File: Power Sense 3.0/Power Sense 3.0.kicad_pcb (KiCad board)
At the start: 2 copper layers, 85.3 x 47.5 mm, 45 parts, among them IC1 MCP3909, J1 Power, J2 ProgHead, J3 SPI, T1 AC1030, T2 Murata_782485_55C, U1 PIC18F25K20_I/SS, Y1 3.579545MHz Crystal

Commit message: Updated files with new files
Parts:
- moved C7 33.6 mm to (108.6, 72.8)
- moved R18 25.9 mm to (117.3, 42.2), turned to 90 degrees
- moved C10 25.1 mm to (131.5, 50.1)
- moved R17 10.9 mm to (114.3, 40.4), turned to 90 degrees
- moved R15 9.01 mm to (131.3, 67.1), turned to 180 degrees
- moved C8 6.48 mm to (113.4, 59.1)
- moved R16 6.35 mm to (115.1, 67.7)
- moved C5 5.76 mm to (102.1, 61.8), turned to 270 degrees
- moved C6 3.54 mm to (101.7, 58.9), turned to 180 degrees
- moved T2 2.79 mm to (73.9, 49.3), turned to 90 degrees
- moved R11 1.59 mm to (102.0, 67.7)
- moved R21 1.28 mm to (122.4, 41.7)
- moved R20 1.21 mm to (122.4, 39.1)
- moved R19 1.15 mm to (122.4, 36.6)
- moved R14 0.83 mm to (105.3, 67.7)
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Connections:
- U1 pad 15: Net-(U1-Pad15) -> Net-(R18-Pad2)
- U1 pad 26: Net-(R18-Pad2) -> Net-(U1-Pad26)
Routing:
- net /+5V: track 0.00 -> 75.5 mm, vias 0 -> 2
- net /Fo0toPIC: track 0.00 -> 68.5 mm, vias 0 -> 2
- net /HFtoPIC: track 0.00 -> 61.1 mm, vias 0 -> 2
- net /LED_TO_11: track 0.00 -> 57.6 mm, vias 0 -> 2
- net /Fo1toPIC: track 0.00 -> 57.3 mm, vias 0 -> 2
- net /LED_TO_12: track 0.00 -> 51.7 mm, vias 0 -> 2
- net Net-(R2-Pad1): track 0.00 -> 49.8 mm
- net Net-(C10-Pad1): track 0.00 -> 49.0 mm, vias 0 -> 2
- net /LED_TO_25: track 0.00 -> 48.4 mm, vias 0 -> 2
- net Net-(R17-Pad2): track 0.00 -> 33.2 mm
- net /SDO: track 0.00 -> 30.3 mm, vias 0 -> 2
- net /SPI_CLK: track 0.00 -> 29.5 mm, vias 0 -> 2
- net /MCLR: track 0.00 -> 29.1 mm, vias 0 -> 2
- net Net-(R3-Pad2): track 0.00 -> 27.9 mm
- net /N: track 0.00 -> 24.2 mm
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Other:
- net class Default: clearance 0.508 -> 0.2032
- net class MCP added: clearance 0.2032, trace_width 0.4064, via_dia 1.6764, via_drill 0.7
- rule trace_clearance: 0.508 -> 0.2032

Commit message: Load Cap Change
Change load capacitors from 30 pF to 27 pF
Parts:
- C8, C9: value 30pF -> 27pF
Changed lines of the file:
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@@
       (effects (font (size 1 1) (thickness 0.15)))
     )
-    (fp_text value 30pF (at 1.25 2.11 270) (layer F.Fab)
+    (fp_text value 27pF (at 1.25 2.11 270) (layer F.Fab)
       (effects (font (size 1 1) (thickness 0.15)))
     )
@@
       (effects (font (size 1 1) (thickness 0.15)))
     )
-    (fp_text value 30pF (at 1.25 2.11 90) (layer F.Fab)
+    (fp_text value 27pF (at 1.25 2.11 90) (layer F.Fab)
       (effects (font (size 1 1) (thickness 0.15)))
     )

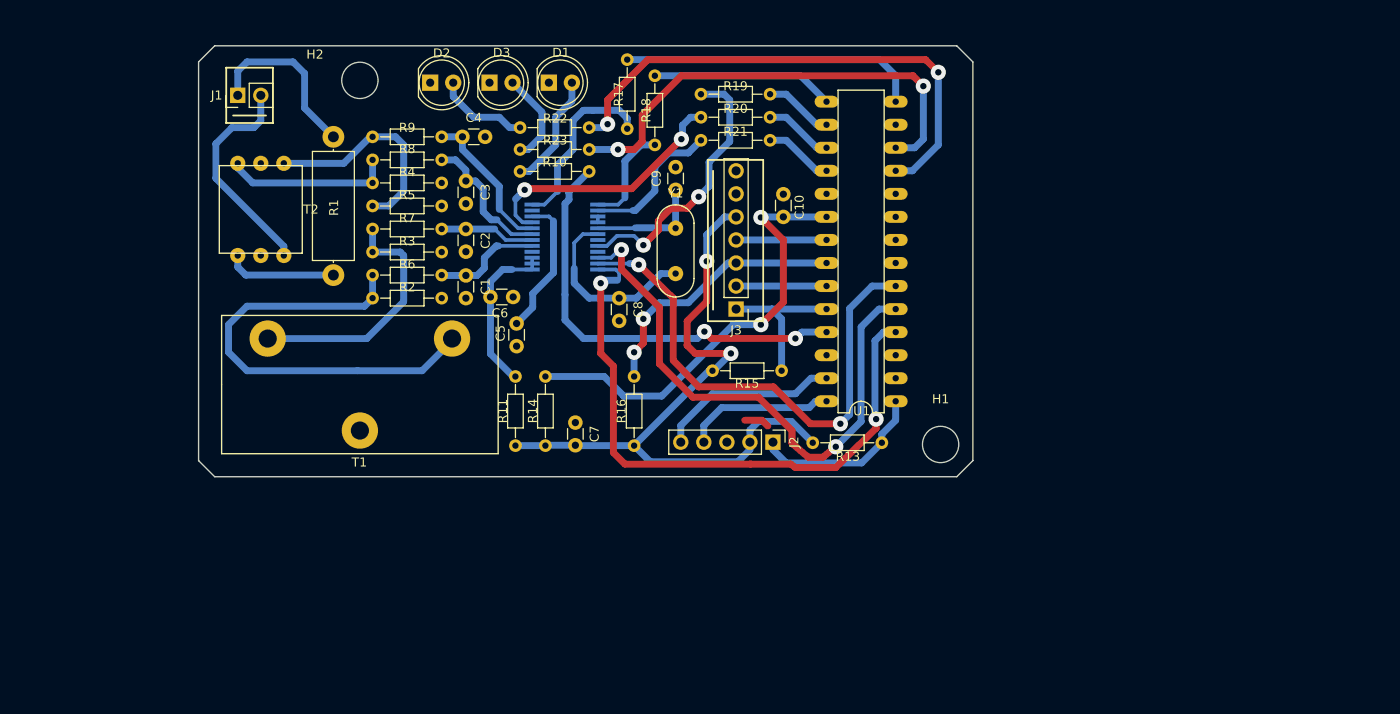
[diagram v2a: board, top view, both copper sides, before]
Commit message: PCB Layout Changes
Increased the width and height of the board slightly. Components were moved, and traces were redone.
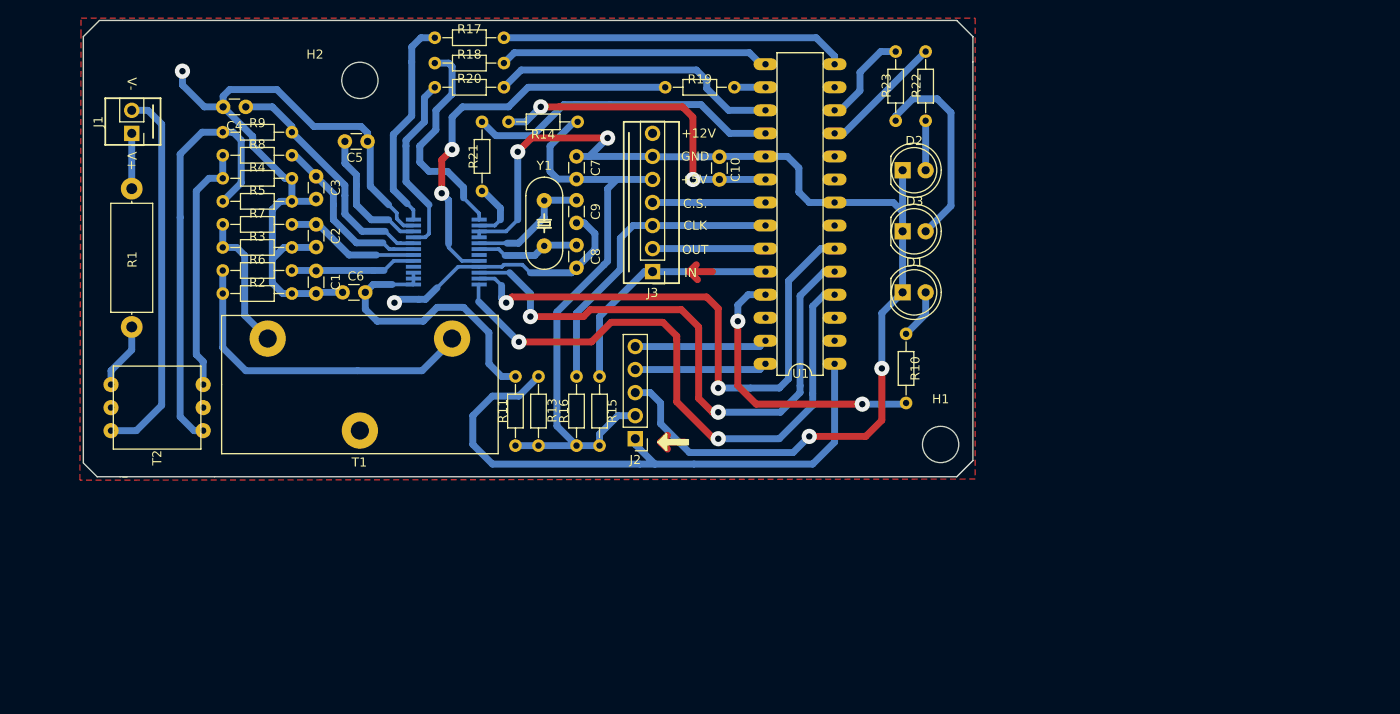
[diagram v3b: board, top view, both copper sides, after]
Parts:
- C8, C9: value 27pF -> 30pF
- moved D2 53.0 mm to (144.7, 45.0)
- moved D3 48.4 mm to (144.7, 51.7)
- moved R10 46.2 mm to (145.0, 63.0), turned to 270 degrees
- moved D1 45.3 mm to (144.7, 58.4)
- moved R22 44.7 mm to (147.2, 39.5), turned to 90 degrees
- moved R23 41.5 mm to (143.9, 39.5), turned to 90 degrees
- moved R13 30.2 mm to (104.5, 75.3), turned to 90 degrees
- moved R20 29.5 mm to (93.1, 35.8)
- moved C7 29.3 mm to (108.7, 43.4)
- moved R14 28.4 mm to (101.2, 39.6), turned to 0 degrees
- moved C5 27.6 mm to (83.2, 41.8), turned to 0 degrees
- moved R18 25.9 mm to (93.1, 33.1), turned to 0 degrees
- moved R21 24.8 mm to (98.3, 47.2), turned to 90 degrees
- moved T2 24.7 mm to (62.5, 71.1), turned to 0 degrees
- moved C4 24.1 mm to (72.3, 38.0), turned to 180 degrees
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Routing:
- net GND: track 0.65 -> 237.6 mm, vias 0 -> 6
- net /5V_PULL_UP: track 19.6 -> 66.3 mm
- net /LED_TO_11: track 57.6 -> 13.8 mm, vias 2 -> 0
- net /LED_TO_12: track 51.7 -> 10.6 mm, vias 2 -> 0
- net Net-(R21-Pad2): track 7.62 -> 34.6 mm
- net Net-(R5-Pad2): track 24.0 -> 47.8 mm
- net Net-(R20-Pad2): track 8.19 -> 32.0 mm
- net /N: track 24.2 -> 41.7 mm
- net /LED_TO_25: track 48.4 -> 31.8 mm
- net Net-(C6-Pad2): track 18.2 -> 32.0 mm
- net /SDO: track 30.3 -> 44.0 mm
- net Net-(R2-Pad1): track 49.8 -> 36.4 mm
- net /H: track 19.3 -> 6.10 mm
- net /SDI: track 11.4 -> 24.3 mm
- net Net-(C10-Pad1): track 49.0 -> 36.3 mm
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- added copper zone on F.Cu, net GND
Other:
- board size 85.3 x 47.5 mm -> 98 x 50.3 mm
- board text added: "+12V"
- board text added: "+5V"
- board text added: "C.S."
- board text added: "CLK"
- board text added: "GND"
- board text added: "IN"
- board text added: "OUT"
- board text added: "V+"
- board text added: "V-"

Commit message: Updated schematic for Power Sense
Updated schematic for Power Sense to include new transformer and resistor divider components.

**Incomplete PCB Layout**
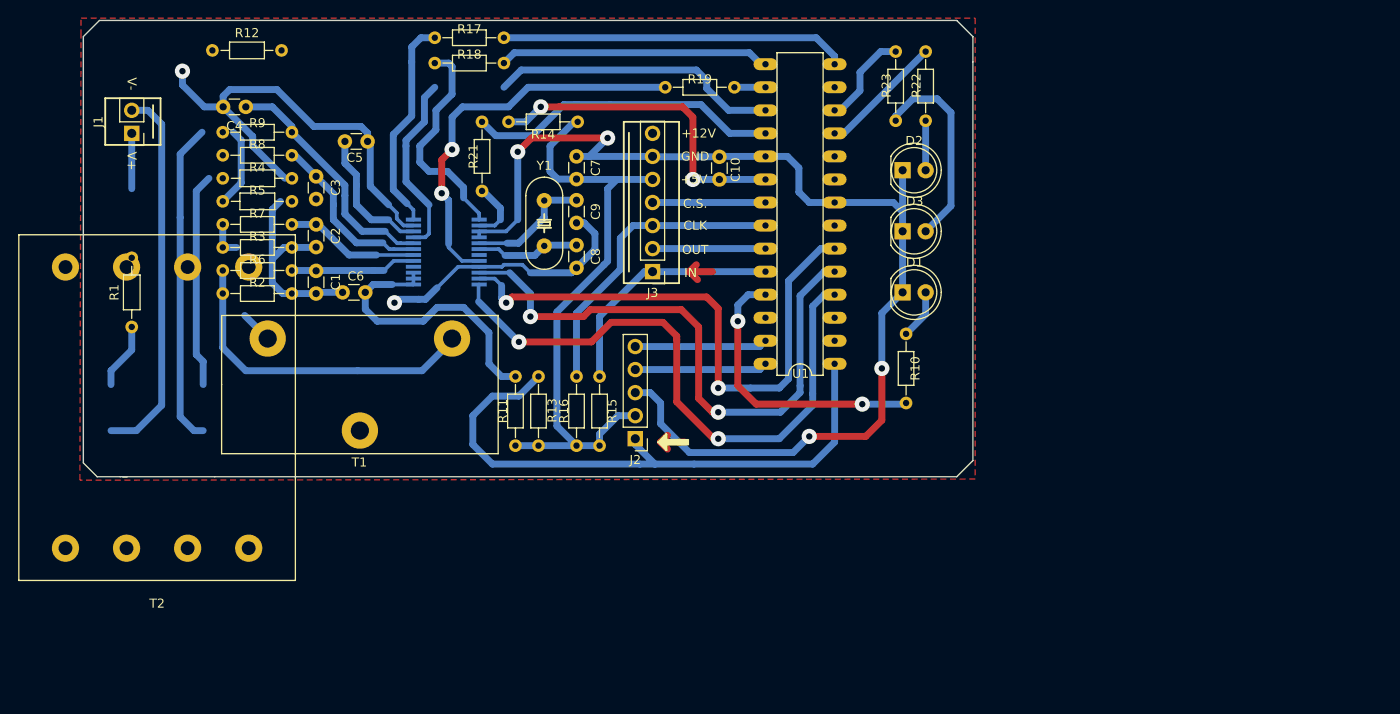
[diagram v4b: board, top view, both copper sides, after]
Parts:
- removed H1, H2: MountingHole_4mm, Mounting_Holes:MountingHole_4mm
- removed R20: 1k, Resistors_THT:R_Axial_DIN0204_L3.6mm_D1.6mm_P7.62mm_Horizontal
- added R12: 1k, Resistor_THT:R_Axial_DIN0204_L3.6mm_D1.6mm_P7.62mm_Horizontal, F.Cu at (68.6, 31.8)
- C8, C9: value 30pF -> 27pF
- R1: value 150k 1W -> 536k; footprint Resistors_THT:R_Axial_DIN0414_L11.9mm_D4.5mm_P15.24mm_Horizontal -> Resistor_THT:R_Axial_DIN0204_L3.6mm_D1.6mm_P7.62mm_Horizontal
- R4: value 200 1% -> 1k; footprint Resistors_THT:R_Axial_DIN0204_L3.6mm_D1.6mm_P7.62mm_Horizontal -> Resistor_THT:R_Axial_DIN0204_L3.6mm_D1.6mm_P7.62mm_Horizontal
- R5: value 200 1% -> 10k 1%; footprint Resistors_THT:R_Axial_DIN0204_L3.6mm_D1.6mm_P7.62mm_Horizontal -> Resistor_THT:R_Axial_DIN0204_L3.6mm_D1.6mm_P7.62mm_Horizontal
- T2: value Murata_782485_55C -> Transformer_1P_1S; footprint EMMS_FP:Murata_782485_Series -> EMMS_FP:Transformer FS12-090-C2
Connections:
- C4 pad 1: Net-(C4-Pad1) -> Net-(C3-Pad2)
- IC1 pad 8: Net-(C4-Pad1) -> Net-(C3-Pad2)
- J1 pad 2: /N -> GND
- R4 pad 1: Net-(R4-Pad1) -> GND
- R4 pad 2: GND -> Net-(R1-Pad1)
- R5 pad 1: GND -> Net-(R1-Pad1)
- R8 pad 1: Net-(R4-Pad1) -> Net-(R1-Pad1)
- R9 pad 1: Net-(R5-Pad2) -> GND
- R9 pad 2: Net-(C4-Pad1) -> Net-(C3-Pad2)
- T2 pad 1: Net-(R1-Pad1) -> /H
- T2 pad 2: Net-(T2-Pad2) -> GND
- T2 pad 3: /N -> GND
- T2 pad 5: Net-(T2-Pad5) -> (no net)
- T2 pad 6: Net-(R4-Pad1) -> (no net)
- U1 pad 17: Net-(R20-Pad2) -> /MCLR
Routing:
- net /N: track 41.7 -> 0.00 mm
- net GND: track 237.6 -> 277.1 mm
- net /MCLR: track 20.4 -> 52.4 mm
- net Net-(R20-Pad2): track 32.0 -> 0.00 mm
- net Net-(C4-Pad1): track 26.9 -> 0.00 mm
- net Net-(C3-Pad2): track 19.4 -> 46.3 mm
- net Net-(R3-Pad2): track 15.5 -> 7.67 mm
- net (no net): track 9.70 -> 4.87 mm
- net Net-(R4-Pad1): track 27.7 -> 23.6 mm
- net Net-(R5-Pad2): track 47.8 -> 44.4 mm

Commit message: Finished Version of initial v3.1
Added connections to all new parts and added silkscreen components
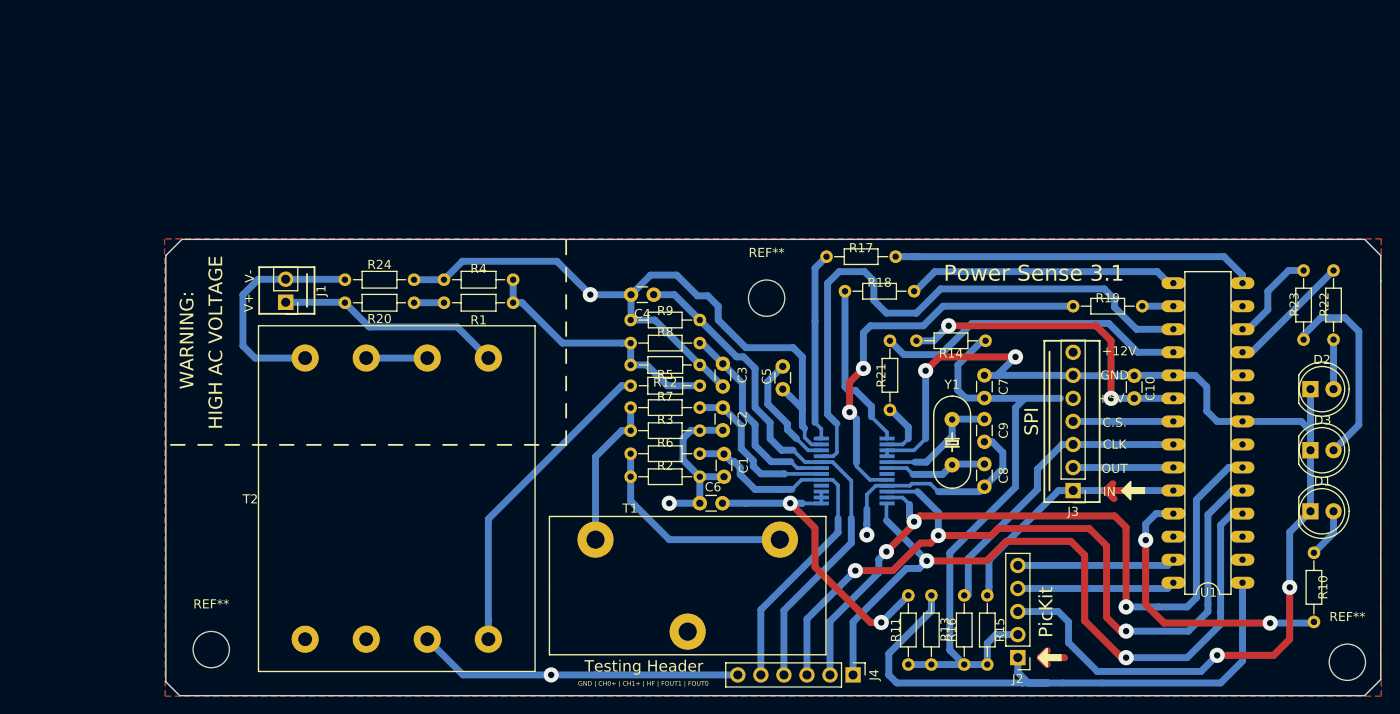
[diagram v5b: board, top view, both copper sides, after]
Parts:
- added J4: TestHeader, Connector_PinHeader_2.54mm:PinHeader_1x06_P2.54mm_Vertical, F.Cu at (139.2, 100.6)
- added R20: 0, Resistor_THT:R_Axial_DIN0204_L3.6mm_D1.6mm_P7.62mm_Horizontal, F.Cu at (90.8, 59.6)
- added R24: 0, Resistor_THT:R_Axial_DIN0204_L3.6mm_D1.6mm_P7.62mm_Horizontal, F.Cu at (90.8, 57.0)
- added REF**: MountingHole_4mm, MountingHole:MountingHole_4mm, F.Cu at (193.7, 99.2)
- added REF**: MountingHole_4mm, MountingHole:MountingHole_4mm, F.Cu at (129.7, 59.1)
- added REF**: MountingHole_4mm, MountingHole:MountingHole_4mm, F.Cu at (68.5, 97.8)
- J3: footprint Pin_Headers:Pin_Header_Straight_1x07_Pitch2.54mm -> Connector_PinHeader_2.54mm:PinHeader_1x07_P2.54mm_Vertical
- T2: value Transformer_1P_1S -> 2p2sTransformer
- moved R12 63.9 mm to (122.3, 66.4), turned to 180 degrees
- moved C5 54.3 mm to (131.4, 66.6), turned to 270 degrees
- moved J3 52.3 mm to (163.4, 80.3)
- moved R18 51.7 mm to (138.3, 58.3)
- moved C10 51.7 mm to (170.2, 70.1)
- moved R19 51.0 mm to (163.4, 59.9)
- moved U1 51.0 mm to (182.1, 90.4)
- moved Y1 51.0 mm to (150.1, 74.9)
- moved D1 51.0 mm to (189.6, 82.5)
- moved D2 51.0 mm to (189.6, 69.1)
- moved D3 51.0 mm to (189.6, 75.8)
- moved R10 51.0 mm to (190.0, 87.1)
- moved R14 51.0 mm to (146.2, 63.8)
- moved R21 51.0 mm to (143.3, 71.4)
- moved R22 51.0 mm to (192.2, 63.6)
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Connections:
- net Net-(C1-Pad2) renamed /CH0+
- C4 pad 1: Net-(C3-Pad2) -> /CH1+
- IC1 pad 8: Net-(C3-Pad2) -> /CH1+
- J1 pad 2: GND -> /N
- R1 pad 2: /H -> Net-(R1-Pad2)
- R9 pad 2: Net-(C3-Pad2) -> /CH1+
- T2 pad 2: GND -> Net-(T2-Pad2)
- T2 pad 3: GND -> Net-(T2-Pad2)
- T2 pad 4: Net-(R5-Pad2) -> /N
- T2 pad 5: (no net) -> Net-(R5-Pad2)
- T2 pad 6: (no net) -> GND
- T2 pad 7: (no net) -> Net-(T2-Pad7)
- T2 pad 8: (no net) -> Net-(T2-Pad8)
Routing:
- net /CH1+: track 0.00 -> 58.3 mm
- net /CH0+: track 13.9 -> 42.4 mm
- net /N: track 0.00 -> 25.0 mm
- net /HFtoPIC: track 64.9 -> 89.4 mm, vias 2 -> 3
- net Net-(C3-Pad2): track 46.3 -> 22.3 mm
- net Net-(R4-Pad1): track 23.6 -> 0.00 mm
- net Net-(R1-Pad1): track 7.30 -> 28.3 mm
- net /Fo1toPIC: track 63.3 -> 84.1 mm, vias 2 -> 3
- net GND: track 277.1 -> 296.5 mm, vias 6 -> 8
- net /H: track 6.10 -> 25.0 mm
- net /Fo0toPIC: track 66.4 -> 83.2 mm
- net /MCLR: track 52.4 -> 66.2 mm
- net Net-(R2-Pad1): track 36.4 -> 23.4 mm
- net Net-(R5-Pad2): track 44.4 -> 35.0 mm
- net Net-(R3-Pad2): track 7.67 -> 16.7 mm
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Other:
- board size 98 x 50.3 mm -> 133.9 x 50.3 mm
- board text added: "GND | CH0+ | CH1+ | HF | FOUT1 | FOUT0"
- board text added: "HIGH AC VOLTAGE"
- board text added: "PicKit"
- board text added: "Power Sense 3.1"
- board text added: "SPI"
- board text added: "Testing Header"
- board text added: "WARNING:"
